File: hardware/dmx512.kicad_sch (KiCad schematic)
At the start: 18 parts, among them J2 B6B-PH-SM4-TB, J3 B6B-PH-SM4-TB, SW1 SW_DIP_x10, U2 MCP23017T-E/SS, U3 CA-IS3092W

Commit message: sorting button and LED
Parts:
- J2, J3: Rotation Offset (none) -> 180; Rotation_offset 180 -> (none)
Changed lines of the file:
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@@
 			)
 		)
-		(property "Rotation_offset" "180"
+		(property "Rotation Offset" "180"
 			(at 38.1 83.82 0)
 			(effects
@@
 			)
 		)
-		(property "Rotation_offset" ""
-			(at 144.78 58.42 0)
-			(effects
-				(font
-					(size 1.27 1.27)
-				)
-				(hide yes)
-			)
-		)
 		(pin "1"
 		)
@@
 			)
 		)
-		(property "Rotation_offset" ""
-			(at 237.49 46.99 0)
-			(effects
-				(font
-					(size 1.27 1.27)
-				)
-				(hide yes)
-			)
-		)
 		(pin "2"
 		)
@@
 			)
 		)
-		(property "Rotation_offset" ""
-			(at 175.26 46.99 0)
-			(effects
-				(font
-					(size 1.27 1.27)
-				)
-				(hide yes)
-			)
-		)
 		(pin "2"
 		)
@@
 			)
 		)
-		(property "Rotation_offset" ""
-			(at 223.52 78.74 0)
-			(effects
-				(font
-					(size 1.27 1.27)
-				)
-				(hide yes)
-			)
-		)
 		(pin "1"
 		)
@@
 			)
 		)
-		(property "Rotation_offset" ""
-			(at 52.07 100.33 90)
-			(effects
-				(font
-					(size 1.27 1.27)
-				)
-				(hide yes)
-			)
-		)
 		(pin "1"
 		)
@@
 			)
 		)
-		(property "Rotation_offset" ""
-			(at 52.07 111.76 90)
-			(effects
-				(font
-					(size 1.27 1.27)
-				)
-				(hide yes)
-			)
-		)
 		(pin "1"
 		)
@@
 			)
 		)
-		(property "Rotation_offset" ""
-			(at 142.24 139.7 0)
-			(effects
-				(font
-					(size 1.27 1.27)
-				)
-				(hide yes)
-			)
-		)
 		(pin "1"
 		)
@@
 			)
 		)
-		(property "Rotation_offset" "180"
+		(property "Rotation Offset" "180"
 			(at 38.1 53.34 0)
 			(effects
@@
 			)
 		)
-		(property "Rotation_offset" ""
-			(at 223.52 46.99 0)
-			(effects
-				(font
-					(size 1.27 1.27)
-				)
-				(hide yes)
-			)
-		)
 		(pin "2"
 		)
@@
 			)
 		)
-		(property "Rotation_offset" ""
-			(at 168.91 142.24 90)
-			(effects
-				(font
-					(size 1.27 1.27)
-				)
-				(hide yes)
-			)
-		)
 		(pin "1"
 		)
@@
 			)
 		)
-		(property "Rotation_offset" ""
-			(at 161.29 46.99 0)
-			(effects
-				(font
-					(size 1.27 1.27)
-				)
-				(hide yes)
-			)
-		)
 		(pin "2"
 		)
@@
 			)
 		)
-		(property "Rotation_offset" ""
-			(at 148.59 109.22 90)
-			(effects
-				(font
-					(size 1.27 1.27)
-				)
-				(hide yes)
-			)
-		)
 		(pin "2"
 		)
@@
 			)
 		)
-		(property "Rotation_offset" ""
-			(at 168.91 129.54 90)
-			(effects
-				(font
-					(size 1.27 1.27)
-				)
-				(hide yes)
-			)
-		)
 		(pin "1"
 		)
@@
 			)
 		)
-		(property "Rotation_offset" ""
-			(at 199.39 67.31 0)
-			(effects
-				(font
-					(size 1.27 1.27)
-				)
-				(hide yes)
-			)
-		)
 		(pin "15"
 		)
@@
 			)
 		)
-		(property "Rotation_offset" ""
-			(at 116.84 76.2 0)
-			(effects
-				(font
-					(size 1.27 1.27)
-				)
-				(hide yes)
-			)
-		)
 		(pin "2"
 		)
@@
 			)
 		)
-		(property "Rotation_offset" ""
-			(at 144.78 73.66 0)
-			(effects
-				(font
-					(size 1.27 1.27)
-				)
-				(hide yes)
-			)
-		)
 		(pin "1"
 		)
@@
 			(at 82.55 154.94 0)
 			(effects
-				(font
-					(size 1.27 1.27)
-				)
-				(hide yes)
-			)
-		)
-		(property "Rotation_offset" ""
-			(at 82.55 154.94 0)
-			(effects

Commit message: starting layout
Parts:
- removed U3: CA-IS3092W, Package_SO:SOIC-16W_7.5x10.3mm_P1.27mm, symbol Interface_UART:ADM2483xRW
- added C23: 100nF, Capacitor_SMD:C_0603_1608Metric, symbol Device:C
- added U6: CA-IS3092VW, Package_SO:SOIC-16W_7.5x10.3mm_P1.27mm, symbol test parts:CA-IS3092VW
- R10, R11: value 4.7k -> 4k7
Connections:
- net +3V3: now also U6.1 (VDD1), U6.7 (VCCL)
- net +3V3_ISO: now also C23.1, U6.14 (VISOIN), U6.16 (VDD2)
- net DMX_DATA+: now also U6.12 (A)
- net DMX_DATA-: now also U6.13 (B)
- net DMX_DE/~{RE}: now also U6.4 (~{RE}), U6.5 (DE)
- net DMX_RX: now also U6.3 (RO)
- net DMX_TX: now also U6.6 (DI)
- net GND: now also U6.2 (GND1), U6.8 (GND1)
- net GND_ISO: now also C23.2, U6.10 (SEL), U6.15 (GND2), U6.9 (GND2)
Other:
- note removed: "Make a symbol for CA-IS3092W CA-IS3092VW"
- note removed: "OUT OF STOCK!"
- moved on the sheet: C5, C7, C8, D1, J2, J3, R10, R11, R43, R8

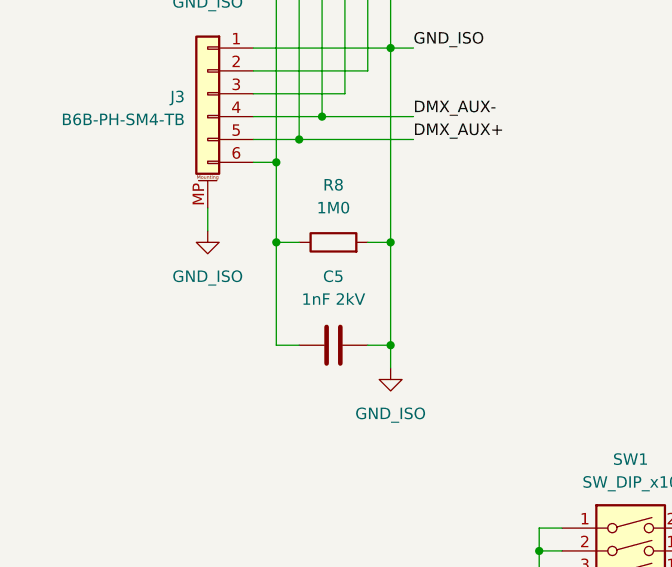
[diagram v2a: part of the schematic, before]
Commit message: adding DRU for DMX isolation
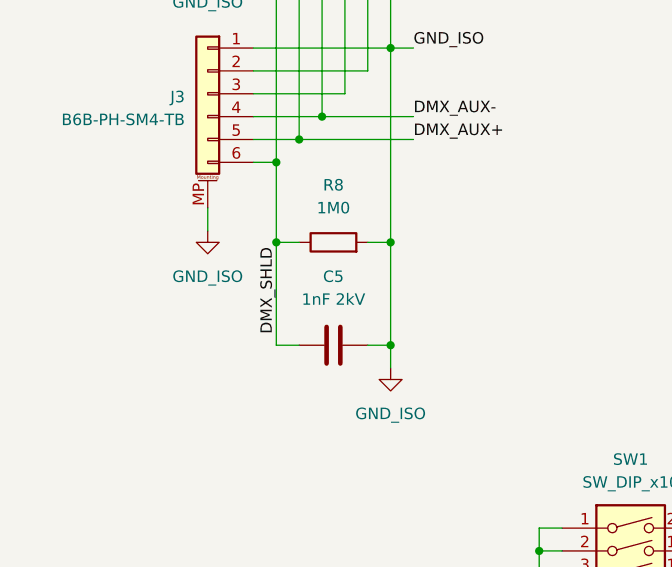
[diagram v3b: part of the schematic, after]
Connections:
- net DMX_SHLD: now reaches C5.1, J2.6 (Pin_6), J3.6 (Pin_6), R8.1
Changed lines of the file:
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@@
+		)
+	)
+	(label "DMX_SHLD"
+		(at 43.18 120.65 90)
+		(effects
+			(font
+				(size 1.27 1.27)
+			)
+			(justify left bottom)
 		)
 	)

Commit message: more layout and fixing OOS items
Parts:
- C10, C23, C5, C6, C7, C8, C9: symbol Device:C -> emf_beacon_ibrary:C
- D1: symbol Diode:SM712_SOT23 -> emf_beacon_ibrary:SM712_SOT23
- J2, J3: symbol Connector_Generic_MountingPin:Conn_01x06_MountingPin -> emf_beacon_ibrary:Conn_01x06_MountingPin
- R10, R11, R12, R13, R43, R8: symbol Device:R -> emf_beacon_ibrary:R
- SW1: symbol Switch:SW_DIP_x10 -> emf_beacon_ibrary:SW_DIP_x10
- U2: symbol Interface_Expansion:MCP23017_SS -> emf_beacon_ibrary:MCP23017_SS
- U6: symbol test parts:CA-IS3092VW -> emf_beacon_ibrary:CA-IS3092VW
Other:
- note added: "I²C Addr: 0x20 MCP23017 has a fault with GPA7 & GPB7. The can corrupt an I²C transaction if they change state during it."
- note removed: "I2C Addr: 0x20"
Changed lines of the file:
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@@
 		(company "Wires & Bits")
 	)
-	(text "I2C Addr: 0x20"
+	(text "I²C Addr: 0x20\nMCP23017 has a fault with GPA7 & GPB7.\nThe can corrupt an I²C transaction if\nthey change state during it."
 		(exclude_from_sim no)
-		(at 141.986 179.832 0)
+		(at 142.494 182.372 0)
 		(effects
 			(font
@@
 	)
 	(symbol
-		(lib_id "Connector_Generic_MountingPin:Conn_01x06_MountingPin")
+		(lib_id "emf_beacon_ibrary:Conn_01x06_MountingPin")
 		(at 35.56 93.98 0)
 		(mirror y)
@@
 	)
 	(symbol
-		(lib_id "Device:R")
+		(lib_id "emf_beacon_ibrary:R")
 		(at 120.65 58.42 0)
 		(unit 1)
@@
 	)
 	(symbol
-		(lib_id "Device:C")
+		(lib_id "emf_beacon_ibrary:C")
 		(at 237.49 46.99 0)
 		(unit 1)
@@
 	)
 	(symbol
-		(lib_id "Device:C")
+		(lib_id "emf_beacon_ibrary:C")
 		(at 161.29 46.99 0)
 		(mirror y)
@@
 	)
 	(symbol
-		(lib_id "Device:R")
+		(lib_id "emf_beacon_ibrary:R")
 		(at 229.87 78.74 0)
 		(unit 1)
@@
 	)
 	(symbol
-		(lib_id "Device:R")
+		(lib_id "emf_beacon_ibrary:R")
 		(at 49.53 110.49 90)
 		(unit 1)
@@
 	)
 	(symbol
-		(lib_id "Device:C")
+		(lib_id "emf_beacon_ibrary:C")
 		(at 49.53 121.92 90)
 		(unit 1)
@@
 	)
 	(symbol
-		(lib_id "Interface_Expansion:MCP23017_SS")
+		(lib_id "emf_beacon_ibrary:MCP23017_SS")
 		(at 142.24 139.7 0)
 		(mirror y)
@@
 	)
 	(symbol
-		(lib_id "Connector_Generic_MountingPin:Conn_01x06_MountingPin")
+		(lib_id "emf_beacon_ibrary:Conn_01x06_MountingPin")
 		(at 35.56 63.5 0)
 		(mirror y)
@@
 	)
 	(symbol
-		(lib_id "Device:C")
+		(lib_id "emf_beacon_ibrary:C")
 		(at 223.52 46.99 0)
 		(unit 1)
@@
 	)
 	(symbol
-		(lib_id "test parts:CA-IS3092VW")
+		(lib_id "emf_beacon_ibrary:CA-IS3092VW")
 		(at 199.39 67.31 0)
 		(mirror y)
@@
 	)
 	(symbol
-		(lib_id "Device:R")
+		(lib_id "emf_beacon_ibrary:R")
 		(at 168.91 142.24 90)
 		(unit 1)
@@
 	)
 	(symbol
-		(lib_id "Device:C")
+		(lib_id "emf_beacon_ibrary:C")
 		(at 147.32 46.99 0)
 		(mirror y)
@@
 	)
 	(symbol
-		(lib_id "Device:C")
+		(lib_id "emf_beacon_ibrary:C")
 		(at 148.59 109.22 270)
 		(mirror x)
@@
 	)
 	(symbol
-		(lib_id "Device:R")
+		(lib_id "emf_beacon_ibrary:R")
 		(at 168.91 129.54 90)
 		(unit 1)
@@
 	)
 	(symbol
-		(lib_id "Device:C")
+		(lib_id "emf_beacon_ibrary:C")
 		(at 175.26 46.99 0)
 		(mirror y)
@@
 	)
 	(symbol
-		(lib_id "Diode:SM712_SOT23")
+		(lib_id "emf_beacon_ibrary:SM712_SOT23")
 		(at 92.71 76.2 0)
 		(unit 1)
@@
 	)
 	(symbol
-		(lib_id "Device:R")
+		(lib_id "emf_beacon_ibrary:R")
 		(at 120.65 73.66 0)
 		(unit 1)
@@
 	)
 	(symbol
-		(lib_id "Switch:SW_DIP_x10")
+		(lib_id "emf_beacon_ibrary:SW_DIP_x10")
 		(at 82.55 154.94 0)
 		(unit 1)

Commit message: updating DMX TRX and improving silkscreen
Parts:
- removed C23: 100nF, Capacitor_SMD:C_0603_1608Metric, symbol emf_beacon_ibrary:C
- U6: value CA-IS3092VW -> CA-IS3092W; LCSC C7422574 -> C2890051
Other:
- note added: "CA-IS3092W has pin 14 as NC but to maintain compatibility with CA-IS3092VW it's connected to 3V3_ISO"
- moved on the sheet: C7, C8

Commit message: preparing for release
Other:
- title: (none) -> DMX512
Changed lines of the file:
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@@
 	(paper "A4")
 	(title_block
-		(date "2026-04-10")
-		(rev "0")
+		(title "DMX512")
+		(date "2026-06-05")
+		(rev "1")
 		(company "Wires & Bits")
 	)
